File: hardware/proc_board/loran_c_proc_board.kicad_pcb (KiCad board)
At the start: 4 copper layers, 170 x 100 mm, 243 parts, among them IC501 PC817, IC502 PC817, J201 RJ45, P101 Power, P102 Cortex SWD, P103 Clock board, P301 UART1 3V3, P302 DB9 Ribbon 2, P303 DB9 Ribbon 1, P304 UART_SEL, P401 SPI Bus A, P402 SPI Bus B, P501 RELAY A, P502 RELAY B, P503 RELAY C, P504 RELAY D, P601 DAC VCO, P602 DAC AGC, P603 QUAD In, P604 LORAN In, Q501 BC847, Q502 BC847, Q503 BC847, Q504 BC847, Q601 BD135, Q602 BD136, U101 LD1117S33, U102 74AC14, U201 LAN8720, U301 ST3232, U302 ST3232, U303 ST3232, U401 74AC14, U402 74AC14, U601 TL072, U602 LD1117S33, U701 STM32F407VG, X201 25MHz, X701 32.768KHz

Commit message: Update: fixed AGND zone on PCB
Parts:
- moved C212 0.06 mm to (220.3, 108.5)
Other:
- rule trace_min: 0.15 -> 0.25
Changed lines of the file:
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@@
   )
   (setup
-    (last_trace_width 0.8)
+    (last_trace_width 0.3)
     (user_trace_width 0.2)
     (user_trace_width 0.25)
@@
     (zone_clearance 0.4)
     (zone_45_only yes)
-    (trace_min 0.15)
+    (trace_min 0.25)
     (segment_width 0.2)
     (edge_width 0.15)
@@
     (mod_text_size 1 1)
     (mod_text_width 0.15)
-    (pad_size 2.2 2.2)
-    (pad_drill 1.3)
+    (pad_size 2.35 2.35)
+    (pad_drill 1.5)
     (pad_to_mask_clearance 0.075)
     (solder_mask_min_width 0.15)
@@
     (visible_elements 7FFFF7FF)
     (pcbplotparams
-      (layerselection 12615681)
+      (layerselection 15761409)
       (usegerberextensions false)
-      (excludeedgelayer true)
+      (excludeedgelayer false)
       (linewidth 0.150000)
-      (plotframeref true)
+      (plotframeref false)
       (viasonmask true)
       (mode 1)
@@
       (psnegative false)
       (psa4output false)
-      (plotreference false)
+      (plotreference true)
       (plotvalue false)
       (plotothertext false)
@@
       (padsonsilk false)
       (subtractmaskfromsilk false)
-      (outputformat 4)
+      (outputformat 1)
       (mirror false)
-      (drillshape 2)
+      (drillshape 0)
       (scaleselection 1)
       (outputdirectory pcb_plots/))
@@
     (at 219.456 96.732 90)
     (tags RJ45)
-    (fp_text reference J201 (at 0.254 4.826 90) (layer F.SilkS)
+    (fp_text reference J201 (at 0.032 1.644 90) (layer F.SilkS)
       (effects (font (thickness 0.3048)))
     )
-    (fp_text value RJ45 (at 0.14224 -0.1016 90) (layer F.SilkS)
+    (fp_text value RJ45 (at 0.032 -1.156 90) (layer F.SilkS)
       (effects (font (size 1.00076 1.00076) (thickness 0.2032)))
     )
@@
     (fp_line (start 7.62 -10.16) (end -7.62 -10.16) (layer F.SilkS) (width 0.127))
     (fp_line (start -7.62 -10.16) (end -7.62 7.874) (layer F.SilkS) (width 0.127))
-    (pad 9 thru_hole circle (at -7.62 3.048 90) (size 2.5 2.5) (drill 1.6) (layers *.Cu *.Mask F.SilkS)
+    (pad 9 thru_hole circle (at -7.62 3.048 90) (size 2.35 2.35) (drill 1.5) (layers *.Cu *.Mask F.SilkS)
       (net 93 GNDPWR))
     (pad Hole thru_hole circle (at 5.93852 0 90) (size 3.5 3.5) (drill 3.5) (layers *.Cu *.Mask F.SilkS))
@@
     (pad 8 thru_hole circle (at 4.445 -8.89 90) (size 1.5 1.5) (drill 0.8) (layers *.Cu *.Mask F.SilkS)
       (net 134 "Net-(J201-Pad7)"))
-    (pad 9 thru_hole circle (at 7.62 3.048 90) (size 2.5 2.5) (drill 1.6) (layers *.Cu *.Mask F.SilkS)
+    (pad 9 thru_hole circle (at 7.62 3.048 90) (size 2.35 2.35) (drill 1.5) (layers *.Cu *.Mask F.SilkS)
       (net 93 GNDPWR))
     (model Connectors/RJ45_8.wrl
@@
   )
   (module w_pth_capacitors:cnp_6mm_disc (layer F.Cu)
-    (at 220.345 108.543)
+    (at 220.3 108.5)
     (descr "6mm disc ceramic capacitor")
     (tags C)
@@
     (at 211.201 84.54 180)
     (descr "SMT resistor, 1206")
-    (fp_text reference R211 (at 0.0254 -1.27 180) (layer F.SilkS)
+    (fp_text reference R211 (at 0.001 -1.46 180) (layer F.SilkS)
       (effects (font (size 0.50038 0.50038) (thickness 0.11938)))
     )
@@
     (at 211.201 82.254 180)
     (descr "SMT resistor, 1206")
-    (fp_text reference R214 (at 0.0254 -1.27 180) (layer F.SilkS)
+    (fp_text reference R214 (at 0.001 1.454 180) (layer F.SilkS)
       (effects (font (size 0.50038 0.50038) (thickness 0.11938)))
     )
@@
   (segment (start 149.6525 99.7) (end 150.224344 99.7) (width 0.25) (layer F.Cu) (net 28) (status 30))
   (segment (start 150.224344 99.7) (end 153.212172 102.687828) (width 0.25) (layer F.Cu) (net 28) (status 30))
-  (segment (start 206.375 92.296) (end 207.908 92.296) (width 0.4) (layer F.Cu) (net 29) (status 10))
-  (segment (start 211.836 97.367) (end 213.106 98.637) (width 0.4) (layer F.Cu) (net 29) (status 20))
-  (segment (start 211.836 94.192) (end 211.836 97.367) (width 0.4) (layer F.Cu) (net 29))
-  (segment (start 211.201 93.557) (end 211.836 94.192) (width 0.4) (layer F.Cu) (net 29))
-  (segment (start 209.169 93.557) (end 211.201 93.557) (width 0.4) (layer F.Cu) (net 29))
-  (segment (start 207.908 92.296) (end 209.169 93.557) (width 0.4) (layer F.Cu) (net 29))
-  (segment (start 206.375 94.836) (end 210.557 94.836) (width 0.4) (layer F.Cu) (net 30) (status 30))
+  (segment (start 206.375 92.296) (end 207.908 92.296) (width 0.3) (layer F.Cu) (net 29) (status 10))
+  (segment (start 207.908 92.296) (end 209.169 93.557) (width 0.3) (layer F.Cu) (net 29))
+  (segment (start 209.169 93.557) (end 211.201 93.557) (width 0.3) (layer F.Cu) (net 29))
+  (segment (start 211.201 93.557) (end 211.836 94.192) (width 0.3) (layer F.Cu) (net 29))
+  (segment (start 211.836 94.192) (end 211.836 97.367) (width 0.3) (layer F.Cu) (net 29))
+  (segment (start 211.836 97.367) (end 213.106 98.637) (width 0.3) (layer F.Cu) (net 29) (status 20))
+  (segment (start 206.375 94.836) (end 210.557 94.836) (width 0.3) (layer F.Cu) (net 30) (status 30))
   (segment (start 188.976 95.217) (end 189 95.193) (width 0.25) (layer F.Cu) (net 31) (status 30))
   (segment (start 189 95.193) (end 189 93.82) (width 0.25) (layer F.Cu) (net 31) (status 10))
@@
   (segment (start 197.993 92.296) (end 196.596 92.296) (width 0.25) (layer F.Cu) (net 32) (status 10))
   (segment (start 189 93.312) (end 196.088 93.312) (width 0.25) (layer F.Cu) (net 32))
-  (segment (start 206.375 98.646) (end 211.21 98.646) (width 0.4) (layer F.Cu) (net 33) (status 10))
-  (segment (start 213.106 100.542) (end 213.106 101.177) (width 0.4) (layer F.Cu) (net 33) (status 30))
-  (segment (start 211.21 98.646) (end 213.106 100.542) (width 0.4) (layer F.Cu) (net 33) (status 20))
-  (segment (start 206.375 101.186) (end 209.287 101.186) (width 0.4) (layer F.Cu) (net 34) (status 10))
-  (segment (start 209.287 101.186) (end 210.566 99.907) (width 0.4) (layer F.Cu) (net 34) (status 20))
+  (segment (start 206.375 98.646) (end 211.21 98.646) (width 0.3) (layer F.Cu) (net 33) (status 10))
+  (segment (start 211.21 98.646) (end 213.106 100.542) (width 0.3) (layer F.Cu) (net 33) (status 20))
+  (segment (start 213.106 100.542) (end 213.106 101.177) (width 0.3) (layer F.Cu) (net 33) (status 30))
+  (segment (start 206.375 101.186) (end 209.287 101.186) (width 0.3) (layer F.Cu) (net 34) (status 10))
+  (segment (start 209.287 101.186) (end 210.566 99.907) (width 0.3) (layer F.Cu) (net 34) (status 20))
   (segment (start 188.976 101.567) (end 189 101.543) (width 0.25) (layer F.Cu) (net 35) (status 30))
   (segment (start 189 101.543) (end 189 100.17) (width 0.25) (layer F.Cu) (net 35) (status 10))
@@
   (segment (start 131.5009 102.9991) (end 131.3 103.2) (width 0.3) (layer F.Cu) (net 92))
   (segment (start 222.504 89.112) (end 222.504 104.352) (width 0.8) (layer B.Cu) (net 93) (status 30))
-  (segment (start 212.344 109.686) (end 216.662 109.686) (width 0.8) (layer F.Cu) (net 94) (status 10))
-  (segment (start 216.662 109.686) (end 217.805 108.543) (width 0.8) (layer F.Cu) (net 94) (status 20))
+  (segment (start 212.344 109.686) (end 216.574 109.686) (width 0.8) (layer F.Cu) (net 94) (status 10))
+  (segment (start 216.574 109.686) (end 217.76 108.5) (width 0.8) (layer F.Cu) (net 94) (status 20))
   (segment (start 205.105 109.686) (end 207.518 109.686) (width 0.8) (layer F.Cu) (net 94) (status 30))
   (segment (start 207.518 109.686) (end 209.931 109.686) (width 0.8) (layer F.Cu) (net 94) (status 30))
@@
   (segment (start 214.63 102.193) (end 214.122 102.701) (width 0.4) (layer F.Cu) (net 133))
   (segment (start 214.63 97.621) (end 214.63 102.193) (width 0.4) (layer F.Cu) (net 133))
-  (segment (start 210.566 97.367) (end 211.836 97.367) (width 0.4) (layer B.Cu) (net 133) (status 10))
-  (segment (start 211.836 97.367) (end 213.106 96.097) (width 0.4) (layer B.Cu) (net 133) (status 20))
+  (segment (start 210.566 97.367) (end 211.836 97.367) (width 0.3) (layer B.Cu) (net 133) (status 10))
+  (segment (start 211.836 97.367) (end 213.106 96.097) (width 0.3) (layer B.Cu) (net 133) (status 20))
   (segment (start 213.106 93.557) (end 215.519 95.97) (width 0.4) (layer F.Cu) (net 134) (status 10))
   (segment (start 209.931 104.479) (end 209.931 106.892) (width 0.4) (layer F.Cu) (net 134) (status 20))
@@
   (segment (start 215.519 95.97) (end 215.519 102.574) (width 0.4) (layer F.Cu) (net 134))
   (segment (start 210.82 92.033) (end 210.566 92.287) (width 0.4) (layer F.Cu) (net 134) (status 30))
-  (segment (start 210.566 92.287) (end 211.836 92.287) (width 0.4) (layer B.Cu) (net 134) (status 10))
-  (segment (start 211.836 92.287) (end 213.106 93.557) (width 0.4) (layer B.Cu) (net 134) (status 20))
+  (segment (start 210.566 92.287) (end 211.836 92.287) (width 0.3) (layer B.Cu) (net 134) (status 10))
+  (segment (start 211.836 92.287) (end 213.106 93.557) (width 0.3) (layer B.Cu) (net 134) (status 20))
   (segment (start 180.6 68.9) (end 179.4002 70.0998) (width 0.3) (layer F.Cu) (net 137))
   (segment (start 196.02 60.12) (end 197.4 61.5) (width 0.3) (layer F.Cu) (net 137))
@@
     (polygon
       (pts
-        (xy 137.3 128.4) (xy 62.9 128.4) (xy 62.9 92.9) (xy 70.9 92.9) (xy 75 88.8)
-        (xy 89.7 88.8) (xy 89.7 91.3) (xy 100.1 91.3) (xy 100.1 83) (xy 111.2 83)
-        (xy 111.2 95.2) (xy 130 95.2) (xy 130 99.1) (xy 127.4 99.1) (xy 127.4 106.6)
-        (xy 131.7 106.6) (xy 132.3 106) (xy 132.3 101.4) (xy 133.2 101.4) (xy 133.2 103)
-        (xy 134.7 103) (xy 135.3 103.6) (xy 135.3 109) (xy 136.2 109.9) (xy 137.3 109.9)
+        (xy 137.3 128.4) (xy 73.4 128.4) (xy 73.4 119.3) (xy 68.8 114.7) (xy 62.9 114.7)
+        (xy 62.9 92.9) (xy 70.9 92.9) (xy 75 88.8) (xy 89.7 88.8) (xy 89.7 91.3)
+        (xy 100.1 91.3) (xy 100.1 83) (xy 111.2 83) (xy 111.2 95.2) (xy 130 95.2)
+        (xy 130 99.1) (xy 127.4 99.1) (xy 127.4 106.6) (xy 131.7 106.6) (xy 132.3 106)
+        (xy 132.3 101.4) (xy 133.2 101.4) (xy 133.2 103) (xy 134.7 103) (xy 135.3 103.6)
+        (xy 135.3 109) (xy 136.2 109.9) (xy 137.3 109.9)
       )
     )

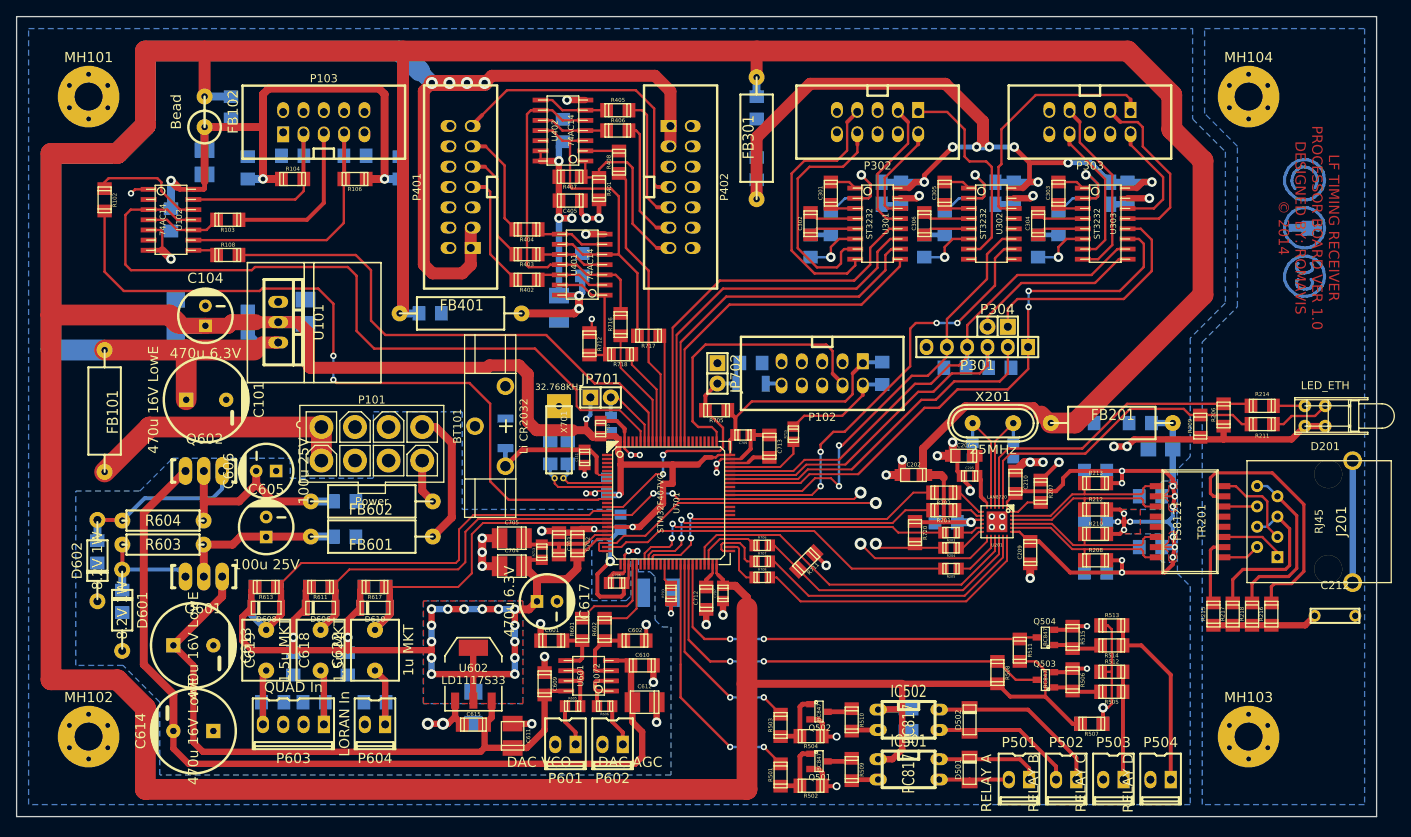
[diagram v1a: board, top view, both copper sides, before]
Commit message: PCB prototype production version, minor schematic updates PCB files sent to PCB house. PCB revision as of this commit can be treated as a first (and, hopefully, last) prototype version
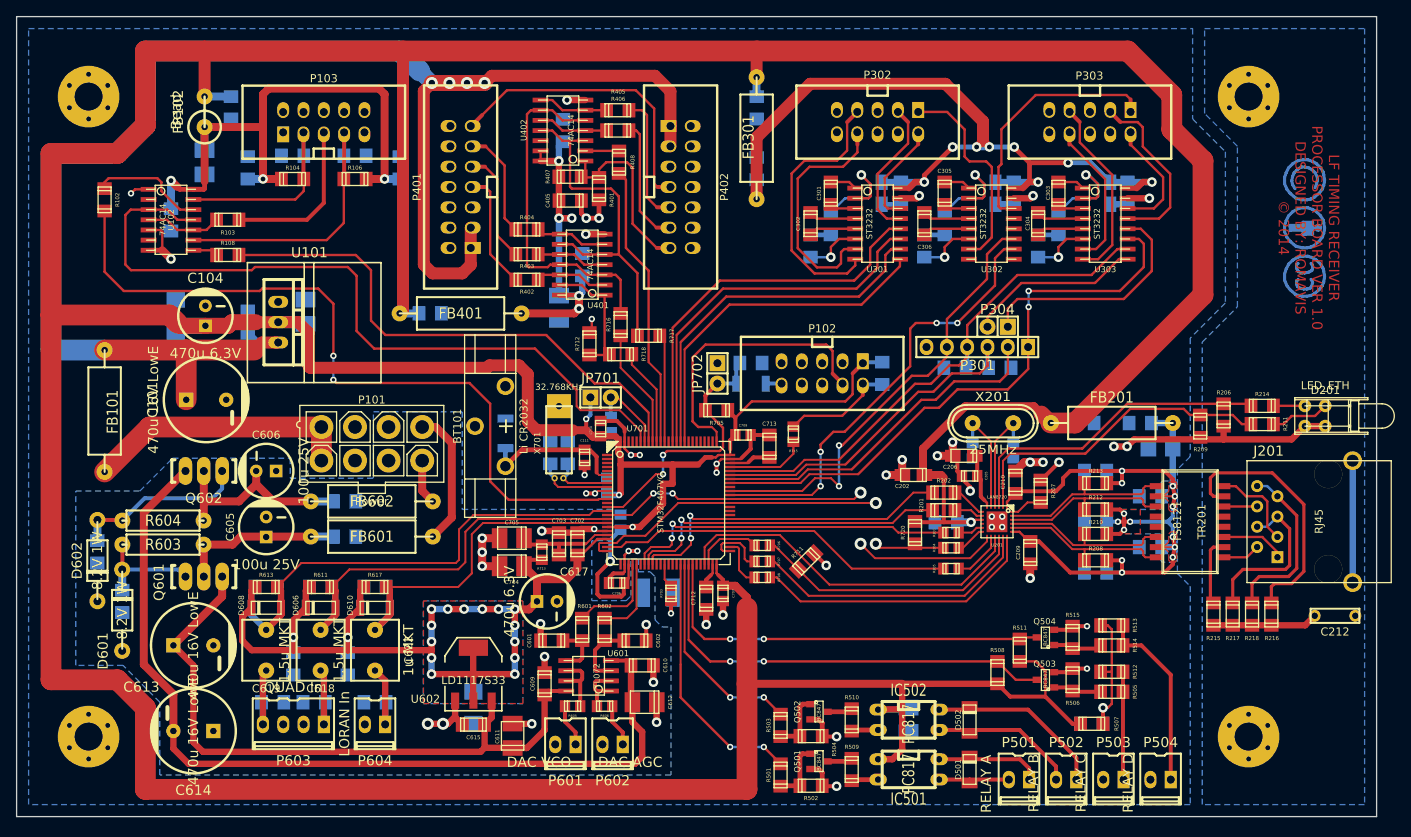
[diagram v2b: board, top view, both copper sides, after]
